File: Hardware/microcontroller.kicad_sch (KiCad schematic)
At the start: 48 parts, among them J1 FTSH-105-X-X-DV-007-P-X, SW1 208-4, U1 STM32F407VGT6, U2 SIT1566AC-JV-XXE-32.768D

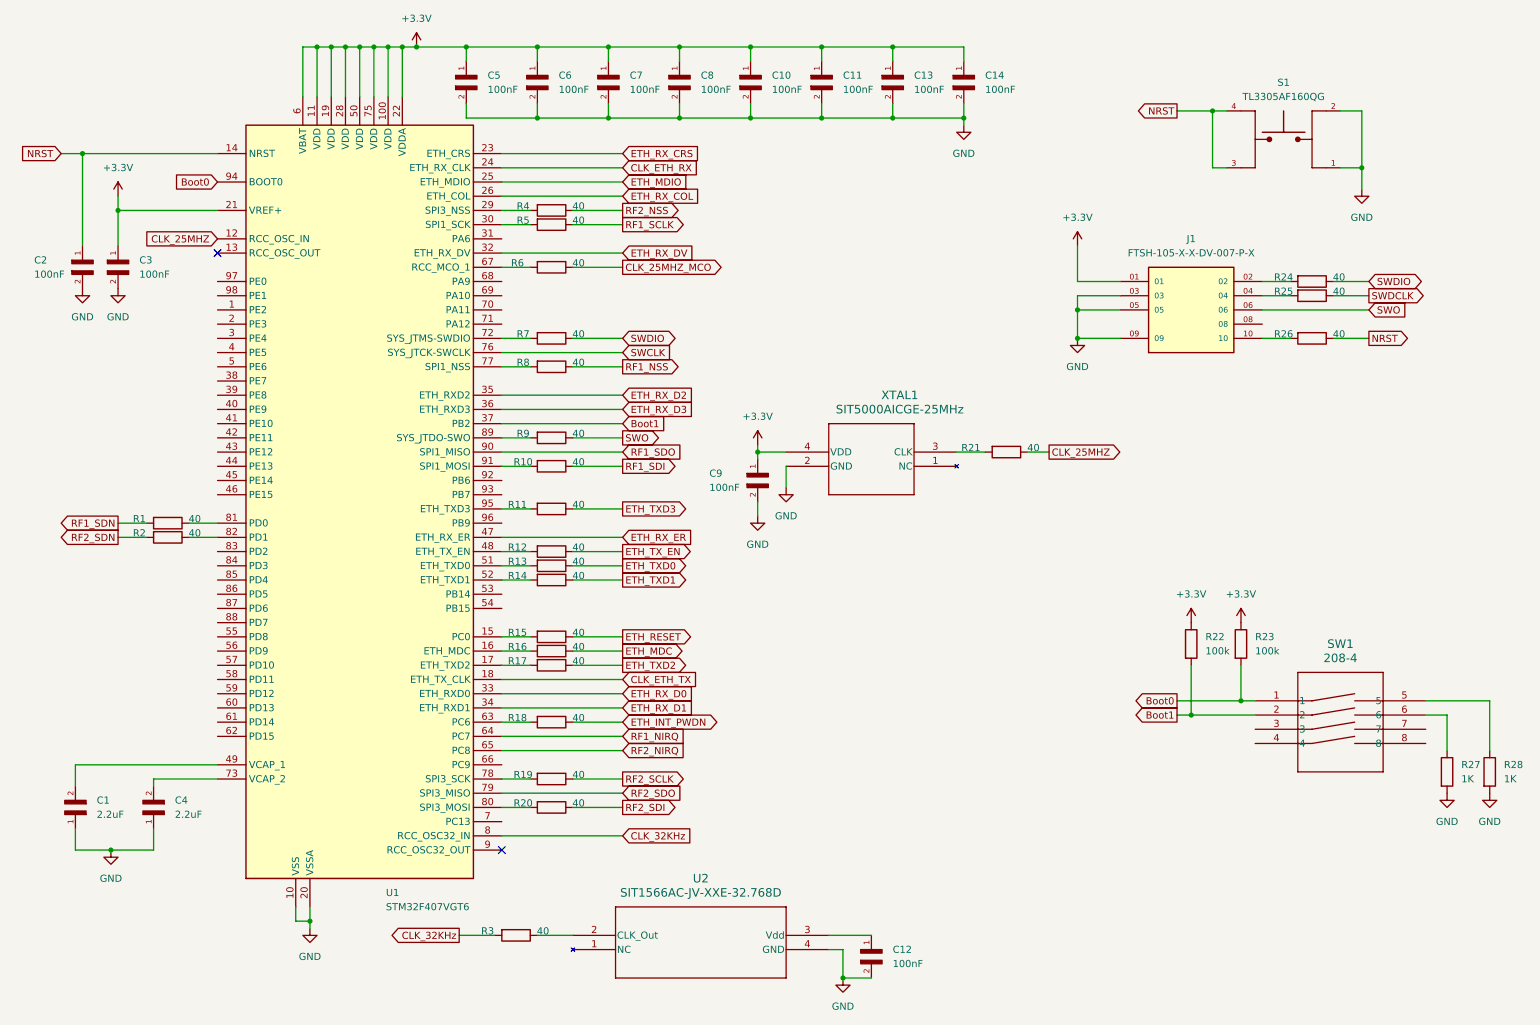
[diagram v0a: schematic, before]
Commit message: added RF matching network and added all 16 layers to stackup
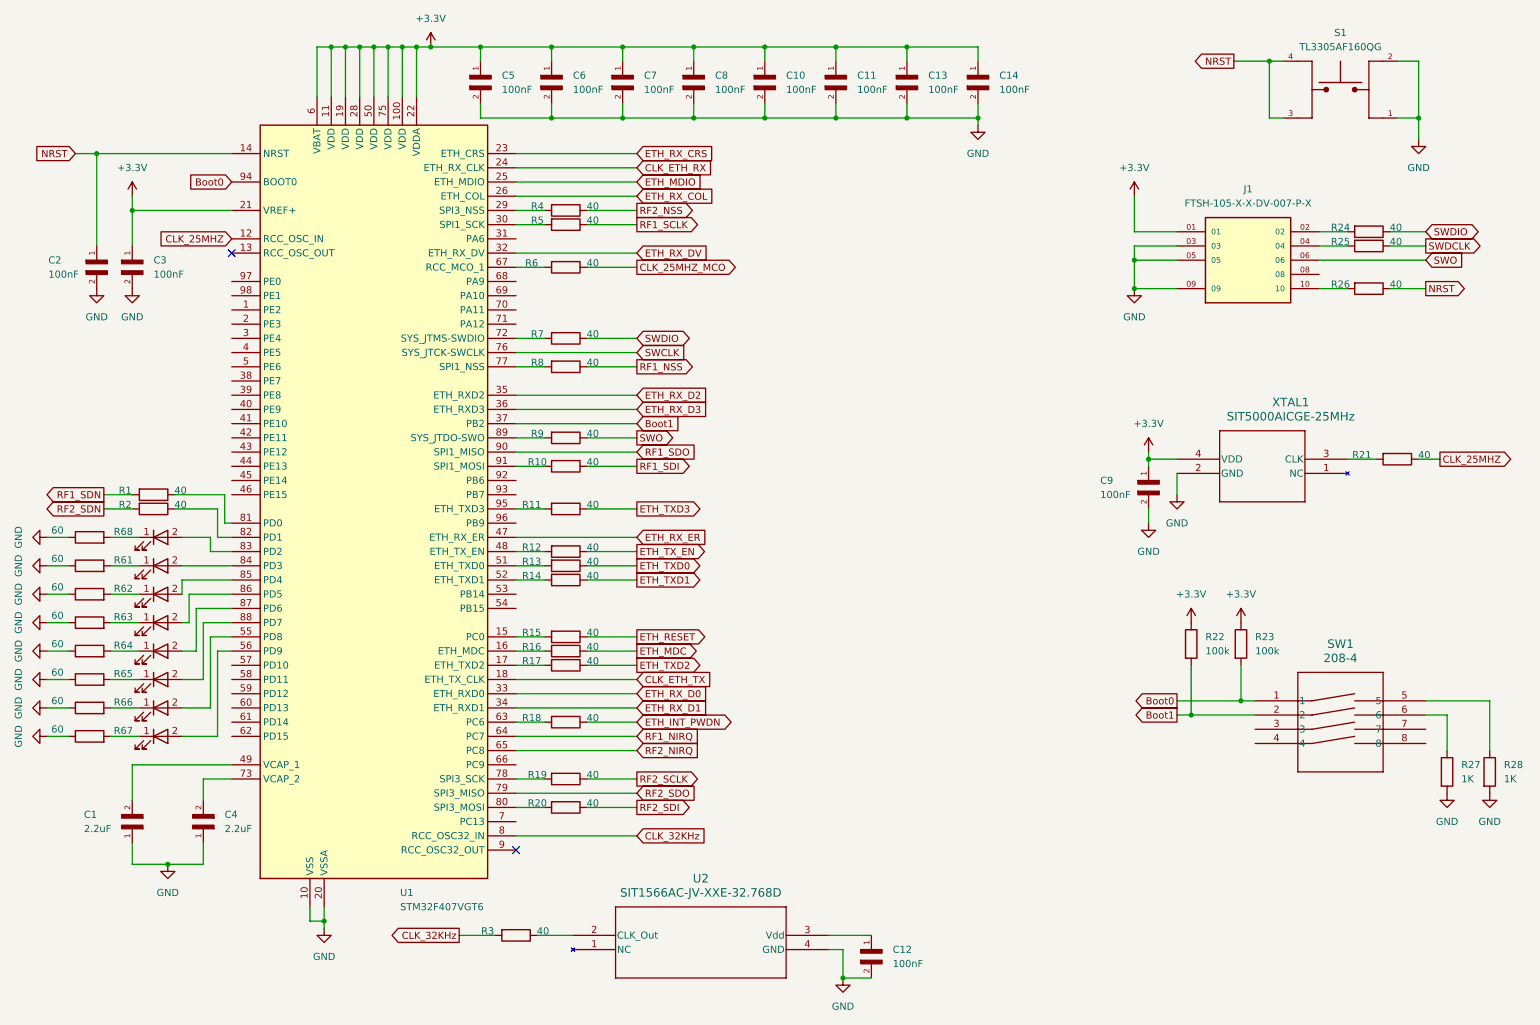
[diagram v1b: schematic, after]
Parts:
- added LED2, LED3, LED4, LED5, LED6, LED7, LED8, LED9: CMD17-21VGD/TR8, CMD17_21VGD_TR8:LED0805N_CML-M, symbol 2025-06-23_02-31-26:CMD17-21VGD_TR8
- added R61, R62, R63, R64, R65, R66, R67, R68: 60, Resistor_SMD:R_0402_1005Metric, symbol Device:R
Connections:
- net GND: now also R61.1, R62.1, R63.1, R64.1, R65.1, R66.1, R67.1, R68.1
- net at U1.55 (PD8): now also LED7.2
- net at U1.56 (PD9): now also LED8.2
- net at U1.83 (PD2): now also LED9.2
- net at U1.84 (PD3): now also LED2.2
- net at U1.85 (PD4): now also LED3.2
- net at U1.86 (PD5): now also LED4.2
- net at U1.87 (PD6): now also LED5.2
- net at U1.88 (PD7): now also LED6.2
- new net: LED7.1, R66.2
- new net: LED6.1, R65.2
- new net: LED4.1, R63.2
- new net: LED2.1, R61.2
- new net: LED8.1, R67.2
- new net: LED5.1, R64.2
- new net: LED9.1, R68.2
- new net: LED3.1, R62.2
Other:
- moved on the sheet: C1, C10, C11, C13, C14, C2, C3, C4, C5, C6, C7, C8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

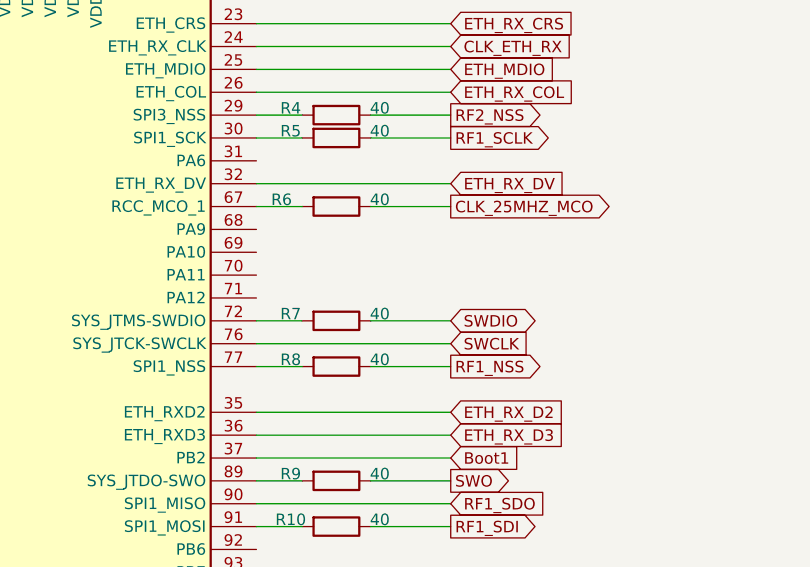
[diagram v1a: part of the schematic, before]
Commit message: connected USB 2.0 data pins
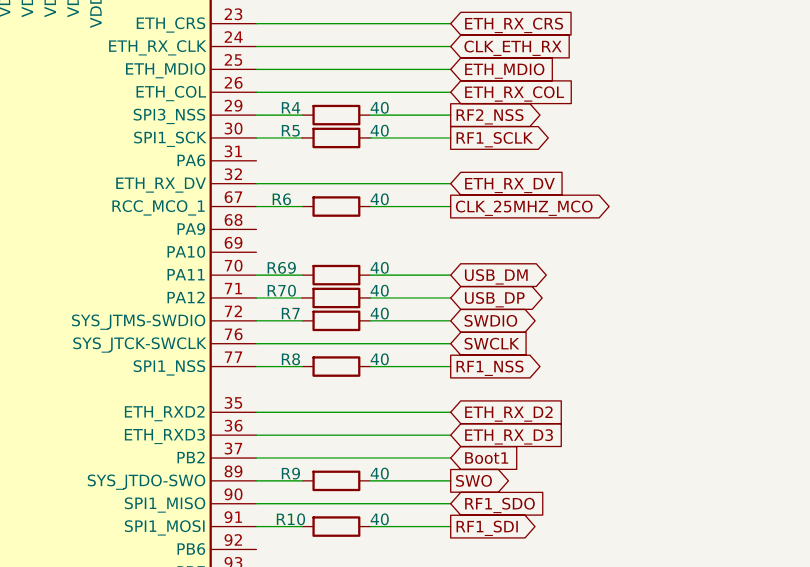
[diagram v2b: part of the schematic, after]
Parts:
- added R69, R70: 40, Resistor_SMD:R_0402_1005Metric, symbol Device:R
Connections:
- net at U1.70 (PA11): now also R69.2
- net at U1.71 (PA12): now also R70.2
- new net USB_DM: R69.1
- new net USB_DP: R70.1
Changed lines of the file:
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@@
 	(wire
 		(pts
+			(xy 102.87 73.66) (xy 107.95 73.66)
+		)
+		(stroke
+			(width 0)
+			(type default)
+		)
+	)
+	(wire
+		(pts
 			(xy 259.08 57.15) (xy 265.43 57.15)
 		)
@@
 	(wire
 		(pts
+			(xy 102.87 71.12) (xy 107.95 71.12)
+		)
+		(stroke
+			(width 0)
+			(type default)
+		)
+	)
+	(wire
+		(pts
 			(xy 34.29 170.18) (xy 40.64 170.18)
 		)
@@
 	(wire
 		(pts
+			(xy 115.57 73.66) (xy 124.46 73.66)
+		)
+		(stroke
+			(width 0)
+			(type default)
+		)
+	)
+	(wire
+		(pts
 			(xy 22.86 142.24) (xy 19.05 142.24)
 		)
@@
 	(wire
 		(pts
+			(xy 115.57 71.12) (xy 124.46 71.12)
+		)
+		(stroke
+			(width 0)
+			(type default)
+		)
+	)
+	(wire
+		(pts
 			(xy 52.07 119.38) (xy 43.18 119.38)
 		)
@@
 		)
 	)
+	(global_label "USB_DM"
+		(shape bidirectional)
+		(at 124.46 71.12 0)
+		(fields_autoplaced yes)
+		(effects
+			(font
+				(size 1.27 1.27)
+			)
+			(justify left)
+		)
+		(property "Intersheetrefs" "${INTERSHEET_REFS}"
+			(at 134.9442 71.12 0)
+			(effects
+				(font
+					(size 1.27 1.27)
+				)
+				(justify left)
+				(hide yes)
+			)
+		)
+	)
 	(global_label "CLK_25MHZ_MCO"
 		(shape output)
@@
 		)
 	)
+	(global_label "USB_DP"
+		(shape bidirectional)
+		(at 124.46 73.66 0)
+		(fields_autoplaced yes)
+		(effects
+			(font
+				(size 1.27 1.27)
+			)
+			(justify left)
+		)
+		(property "Intersheetrefs" "${INTERSHEET_REFS}"
+			(at 134.7628 73.66 0)
+			(effects
+				(font
+					(size 1.27 1.27)
+				)
+				(justify left)
+				(hide yes)
+			)
+		)
+	)
 	(global_label "ETH_INT_PWDN"
 		(shape bidirectional)
@@
 	)
 	(symbol
+		(lib_id "Device:R")
+		(at 111.76 71.12 270)
+		(unit 1)
+		(exclude_from_sim no)
+		(in_bom yes)
+		(on_board yes)
+		(dnp no)
+		(property "Reference" "R69"
+			(at 105.664 70.358 90)
+			(effects
+				(font
+					(size 1.27 1.27)
+				)
+			)
+		)
+		(property "Value" "40"
+			(at 116.586 70.358 90)
+			(effects
+				(font
+					(size 1.27 1.27)
+				)
+			)
+		)
+		(property "Footprint" "Resistor_SMD:R_0402_1005Metric"
+			(at 111.76 69.342 90)
+			(effects
+				(font
+					(size 1.27 1.27)
+				)
+				(hide yes)
+			)
+		)
+		(property "Datasheet" "~"
+			(at 111.76 71.12 0)
+			(effects
+				(font
+					(size 1.27 1.27)
+				)
+				(hide yes)
+			)
+		)
+		(property "Description" "Resistor"
+			(at 111.76 71.12 0)
+			(effects
+				(font
+					(size 1.27 1.27)
+				)
+				(hide yes)
+			)
+		)
+		(pin "1"
+		)
+		(pin "2"
+		)
+		(instances
+			(project "Radio Project"
+				(path "/ca6389fe-9846-40e3-87a4-456cfcfc0777/ea821ff4-3fef-400e-81c9-25868b35804d"
+					(reference "R69")
+					(unit 1)
+				)
+			)
+		)
+	)
+	(symbol
 		(lib_id "power:GND")
 		(at 19.05 116.84 270)
@@
 					(unit 1)
 				)
+			)
+		)
+	)
+	(symbol
+		(lib_id "Device:R")
+		(at 111.76 73.66 270)
+		(unit 1)
+		(exclude_from_sim no)
+		(in_bom yes)
+		(on_board yes)
+		(dnp no)
+		(property "Reference" "R70"
+			(at 105.664 72.898 90)
+			(effects
+				(font
+					(size 1.27 1.27)
+				)
+			)
+		)
+		(property "Value" "40"
+			(at 116.586 72.898 90)
+			(effects
+				(font
+					(size 1.27 1.27)
+				)
+			)
+		)
+		(property "Footprint" "Resistor_SMD:R_0402_1005Metric"
+			(at 111.76 71.882 90)
+			(effects
+				(font
+					(size 1.27 1.27)
+				)
+				(hide yes)
+			)
+		)
+		(property "Datasheet" "~"
+			(at 111.76 73.66 0)
+			(effects
+				(font
+					(size 1.27 1.27)
+				)
+				(hide yes)
+			)
+		)
+		(property "Description" "Resistor"
+			(at 111.76 73.66 0)
+			(effects
+				(font
+					(size 1.27 1.27)
+				)
+				(hide yes)
+			)
+		)
+		(pin "1"
+		)
+		(pin "2"
+		)
+		(instances
+			(project "Radio Project"
+				(path "/ca6389fe-9846-40e3-87a4-456cfcfc0777/ea821ff4-3fef-400e-81c9-25868b35804d"
+					(reference "R70")
+					(unit 1)
+				)
